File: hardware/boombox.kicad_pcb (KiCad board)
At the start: 4 copper layers, 125 x 91.5 mm, 87 parts, among them J1 Micro_SD_Card_Det1, J2 AudioJack4, J3 Battery, J4 USB_C_Receptacle_USB2.0_16P, SW1 SW_SPST, SW2 SW_SPST, SW3 SW_SPST, SW4 SW_SPST, SW5 SW_SPST, U1 Pico, U10 MAX98365A, U2 TMAG5231, U3 TMAG5231, U4 TMAG5231, U5 TMAG5231, U6 TMAG5231, U7 MCP7940MT-I/SN, U8 MAX98365A, U9 MCP73811T-420I-OT, Y1 Crystal

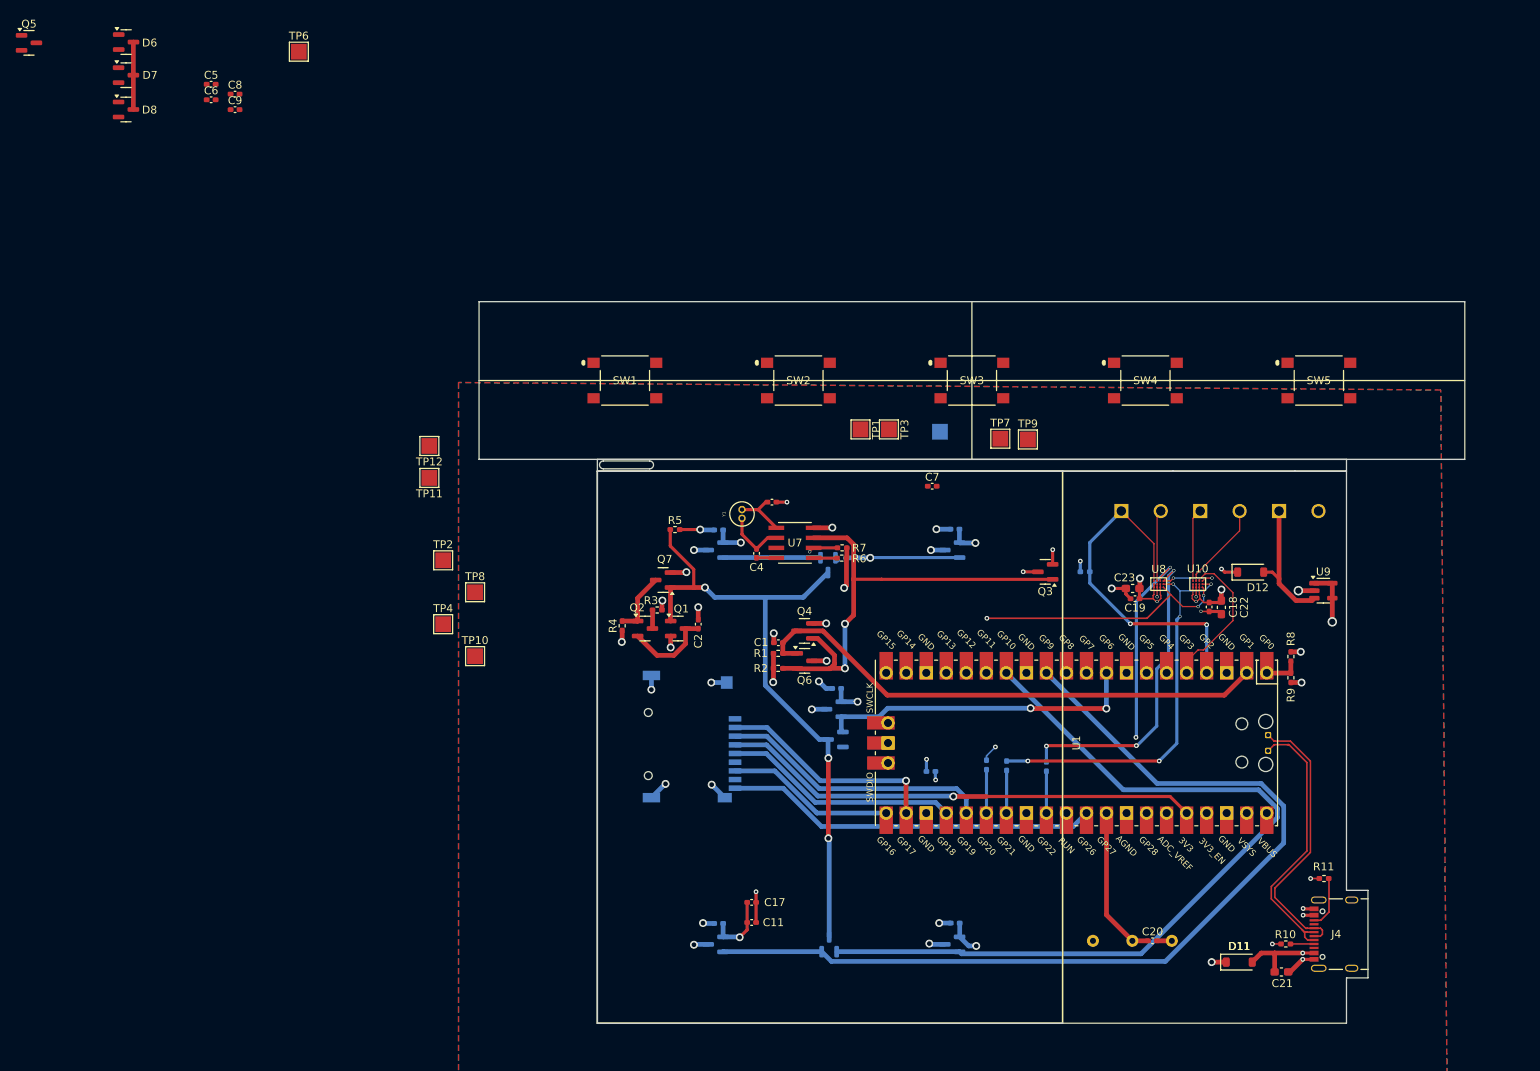
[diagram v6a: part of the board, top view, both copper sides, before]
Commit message: Resized cartridge and moved around things
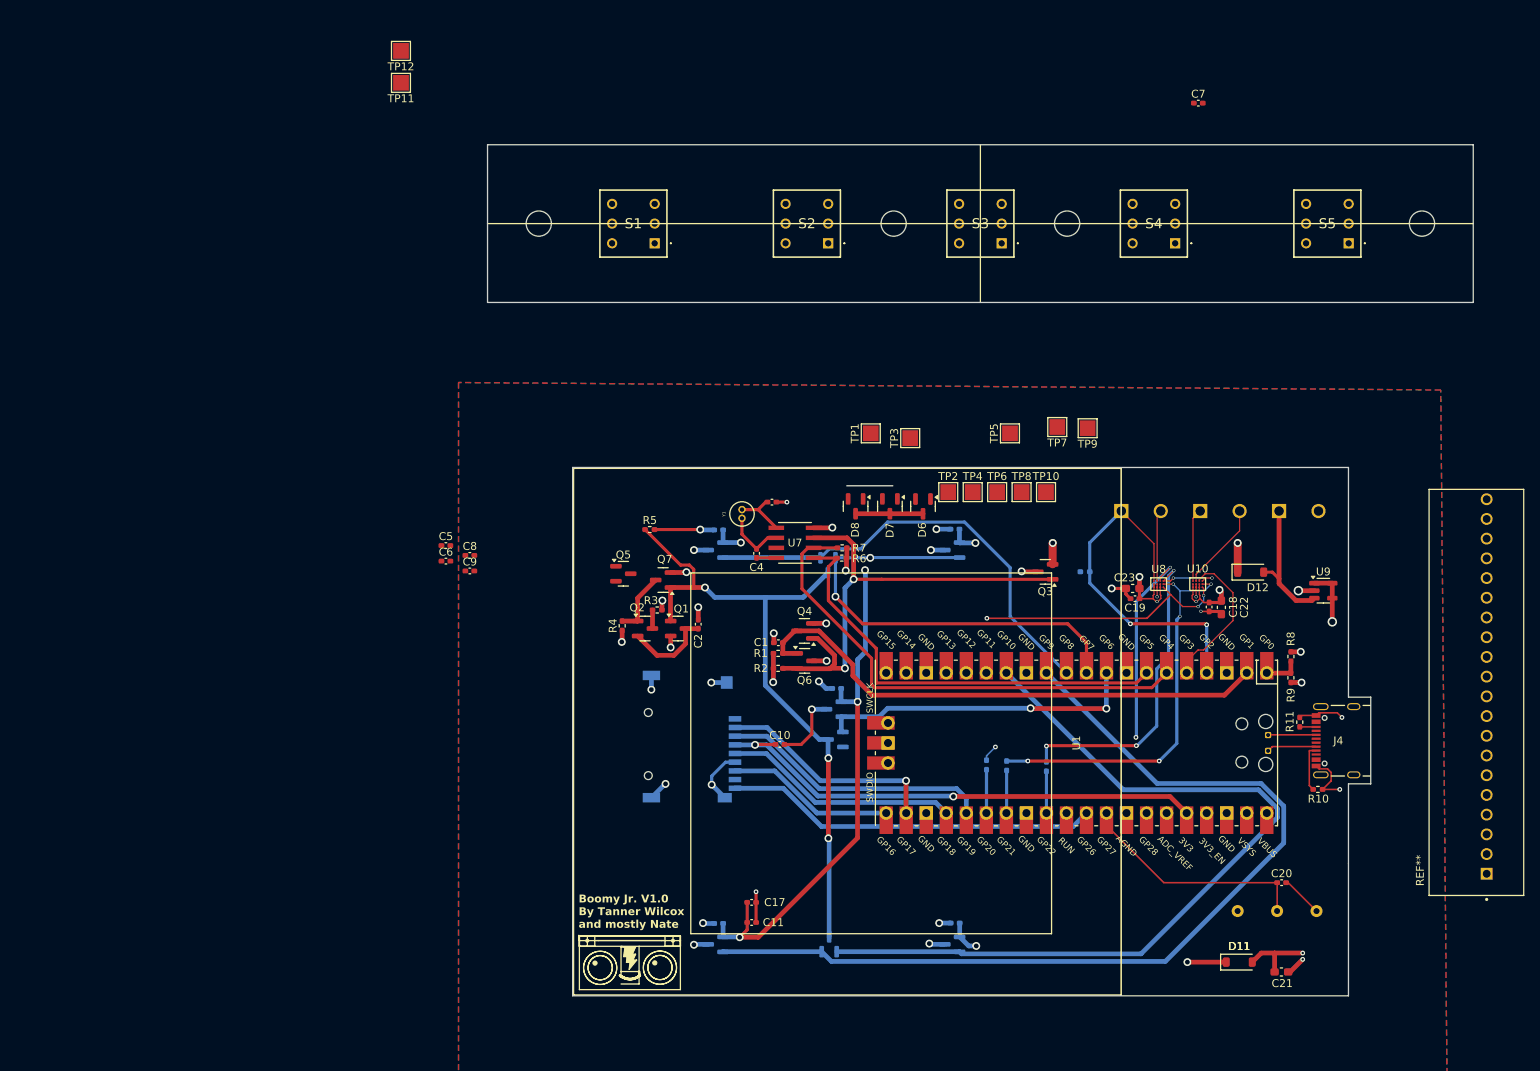
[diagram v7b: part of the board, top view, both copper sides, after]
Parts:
- removed SW1, SW2, SW3, SW4, SW5: SW_SPST, boombox:PTS645S_SMTR92_CNK
- added REF**: MountingHole_3.2mm_M3, MountingHole:MountingHole_3.2mm_M3, F.Cu at (99.0, 36.4)
- added REF**: MountingHole_3.2mm_M3, MountingHole:MountingHole_3.2mm_M3, F.Cu at (211.0, 36.4)
- added REF**: MountingHole_3.2mm_M3, MountingHole:MountingHole_3.2mm_M3, F.Cu at (166.0, 36.4)
- added REF**: PHOENIX_1989926, boombox:PHOENIX_1989926, F.Cu at (223.9, 121.6)
- added REF**: MountingHole_3.2mm_M3, MountingHole:MountingHole_3.2mm_M3, F.Cu at (144.0, 36.4)
- added S1: TL2202OAYA, boombox:TL2202OAYA, F.Cu at (111.0, 36.4)
- added S2: TL2202OAYA, boombox:TL2202OAYA, F.Cu at (133.0, 36.4)
- added S3: TL2202OAYA, boombox:TL2202OAYA, F.Cu at (155.0, 36.4)
- added S4: TL2202OAYA, boombox:TL2202OAYA, F.Cu at (177.0, 36.4)
- added S5: TL2202OAYA, boombox:TL2202OAYA, F.Cu at (199.0, 36.4)
- C10, TP5: moved to F.Cu
- moved D6 117.0 mm to (147.7, 72.3), turned to -90 degrees
- moved D7 111.2 mm to (143.5, 72.2), turned to -90 degrees
- moved D8 105.3 mm to (139.2, 72.2), turned to -90 degrees
- moved TP6 104.7 mm to (157.1, 70.5)
- moved Q5 101.1 mm to (109.7, 80.8)
- moved TP10 75.3 mm to (163.3, 70.5)
- moved TP8 70.5 mm to (160.2, 70.5)
- moved TP4 69.2 mm to (154.0, 70.5)
- moved C5 65.6 mm to (87.2, 77.2)
- moved C6 65.6 mm to (87.2, 79.2)
- moved C8 65.6 mm to (90.2, 78.5)
- moved C9 65.6 mm to (90.2, 80.5)
- moved TP2 64.6 mm to (150.9, 70.5)
- moved C7 59.1 mm to (182.6, 21.1)
- moved TP11 50.2 mm to (81.5, 18.6)
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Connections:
- D8 pad 1: /Power/BUTTONS0 -> (no net)
- D8 pad 3: Net-(D6A-K) -> unconnected-(D8B-K-Pad3)
- Q2 pad 3: Net-(D6A-K) -> /Power/BUTTONS0
- Q5 pad 1: Net-(D6A-K) -> /Power/BUTTONS0
- R3 pad 1: Net-(D6A-K) -> /Power/BUTTONS0
- TP1 pad 1: Net-(SW1-A) -> Net-(S1-NC_1)
- TP10 pad 1: /Power/BUTTONS4 -> /Power/BUTTONS0
- TP3 pad 1: Net-(SW2-A) -> Net-(S2-NC_1)
- TP4 pad 1: /Power/BUTTONS1 -> /Power/BUTTONS0
- TP5 pad 1: Net-(SW3-A) -> Net-(S3-NC_1)
- TP6 pad 1: /Power/BUTTONS2 -> /Power/BUTTONS0
- TP7 pad 1: Net-(SW4-A) -> Net-(S4-NC_1)
- TP8 pad 1: /Power/BUTTONS3 -> /Power/BUTTONS0
- TP9 pad 1: Net-(SW5-A) -> Net-(S5-NC_1)
- U1 pad 15: Net-(SW1-A) -> Net-(S1-NC_2)
- U1 pad 16: Net-(SW2-A) -> Net-(S2-NC_2)
- U1 pad 17: Net-(SW3-A) -> Net-(S3-NC_2)
- U1 pad 19: Net-(SW4-A) -> Net-(S4-NC_2)
- U1 pad 20: Net-(SW5-A) -> Net-(S5-NC_2)
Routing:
- net VCC: track 246.4 -> 24.1 mm, vias 7 -> 6
- net Net-(U1-GPIO4): track 3.73 -> 63.4 mm, vias 1 -> 0
- net Net-(U1-GPIO5): track 2.98 -> 56.6 mm
- net /Power/MAG_SENSOR2: track 12.4 -> 57.0 mm
- net /Power/MAG_SENSOR1: track 17.1 -> 60.9 mm, vias 1 -> 2
- net /USB_DP: track 35.4 -> 6.11 mm
- net /USB_DN: track 35.2 -> 6.32 mm
- net GND: track 70.1 -> 94.9 mm, vias 33 -> 31
- net SLP_PWR: track 244.3 -> 265.8 mm, vias 12 -> 13
- net /Audio/VOL: track 19.5 -> 29.8 mm
- net /Power/POWER IN: track 70.3 -> 65.3 mm, vias 4 -> 3
- net Net-(J4-CC2): track 6.59 -> 2.08 mm
- net Net-(J4-CC1): track 2.99 -> 5.97 mm
- net Net-(D6A-K): track 10.9 -> 8.56 mm
- net /Power/BUTTONS0: track 0.00 -> 2.36 mm
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- added copper zone on In2.Cu, net VCC
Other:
- board size 125 x 91.5 mm -> 125 x 107.9 mm
- board text added: "Boomy Jr. V1.0 By Tanner Wilcox and mostly Nate"

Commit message: Resizing
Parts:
- REF**: moved to B.Cu
- moved REF** 55.5 mm to (199.7, 71.7), turned to -90 degrees
- moved J4 3.16 mm to (204.5, 102.0)
- moved R11 2.93 mm to (198.4, 99.5)
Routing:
- net GND: track 94.9 -> 84.2 mm
- net /USB_DP: track 6.11 -> 0.00 mm
- net /USB_DN: track 6.32 -> 9.48 mm
- net Net-(J4-CC2): track 2.08 -> 0.00 mm
- net Net-(J4-CC1): track 5.97 -> 7.47 mm
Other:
- outline, holes or cut-outs redrawn
- board text added: "Boomy Jr. V1.0"
- board text removed: "Boomy Jr. V1.0 By Tanner Wilcox and mostly Nate"
